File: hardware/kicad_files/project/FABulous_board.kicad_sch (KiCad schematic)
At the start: 7 parts, among them SW1 Tactile Switch

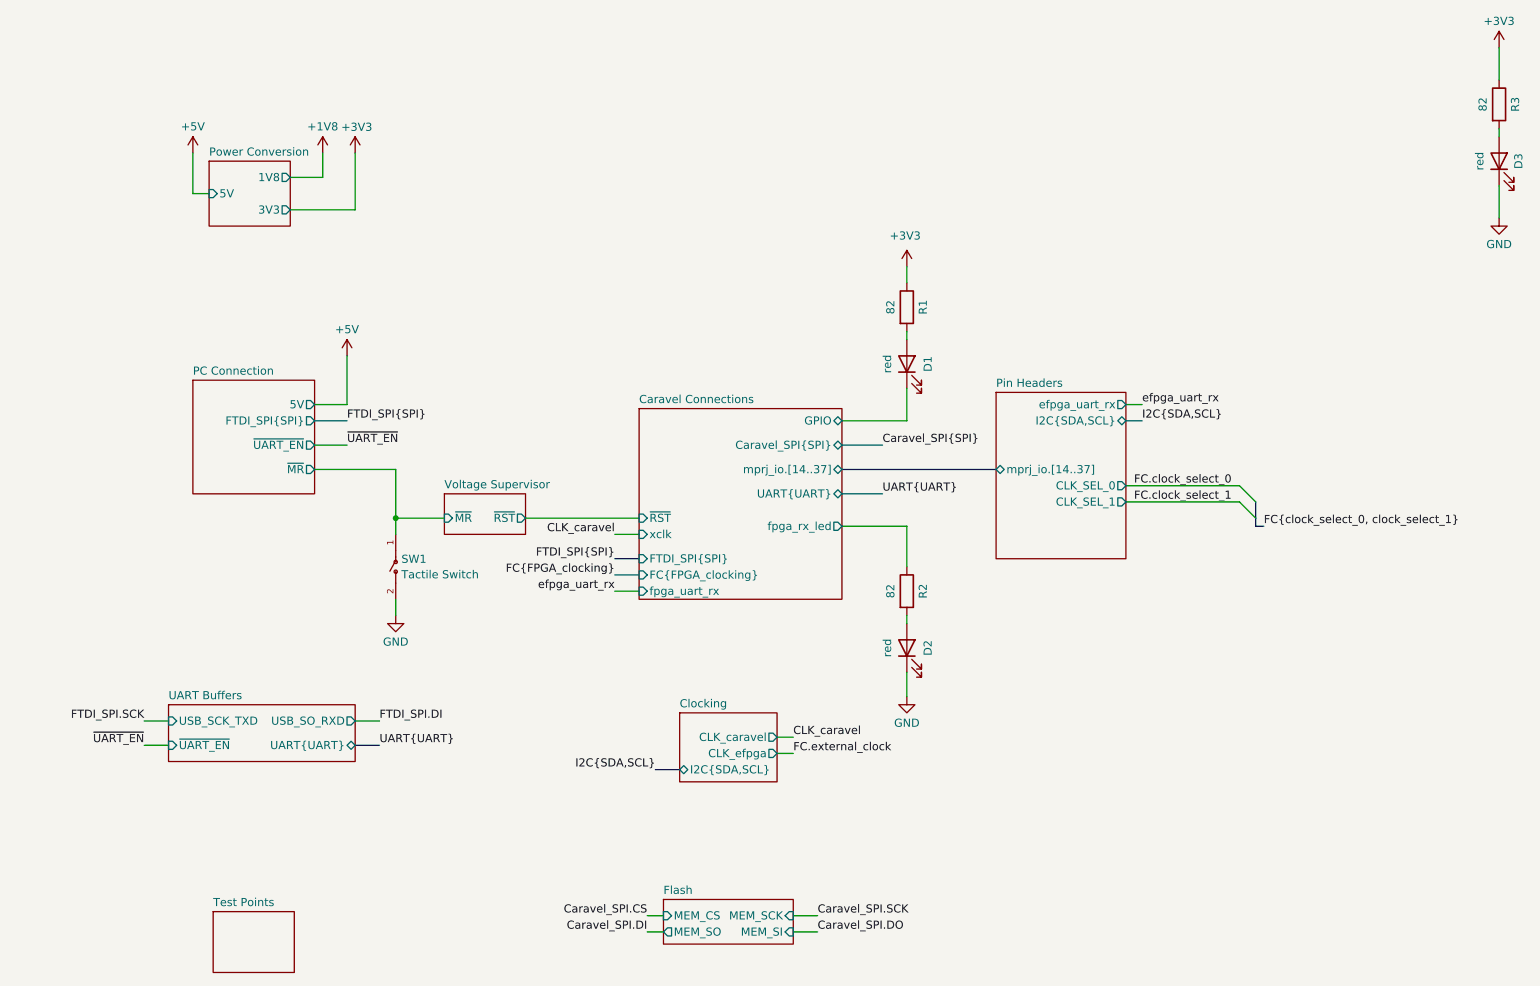
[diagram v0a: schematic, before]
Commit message: feat: optimize layout, reassign annotations, add 2x4 header for UART selection
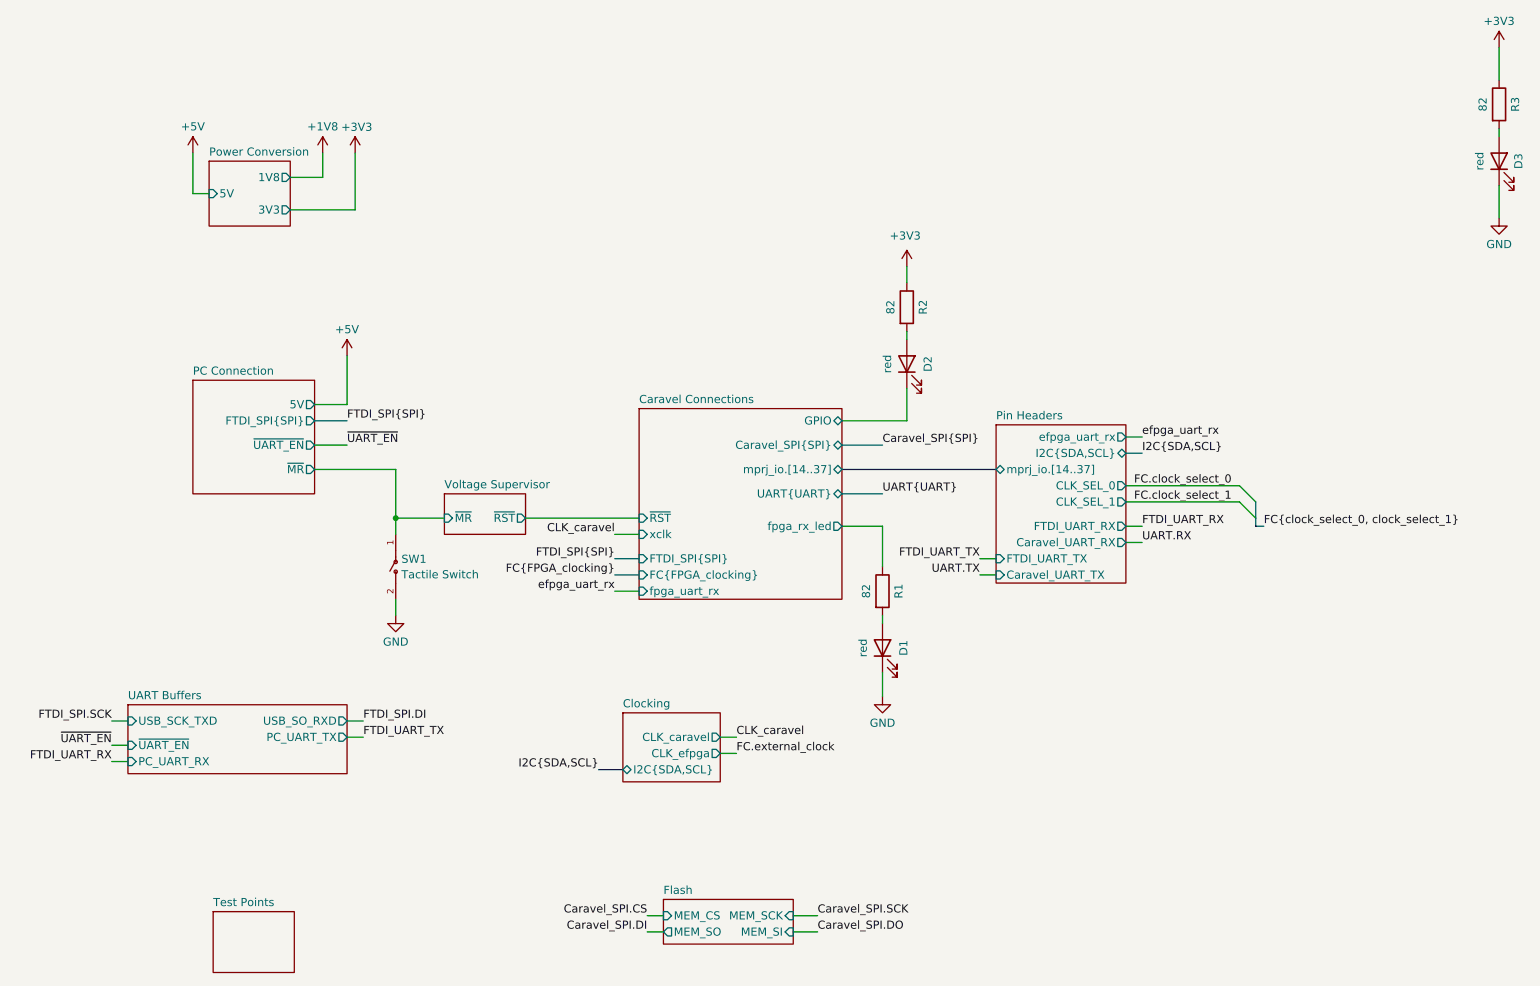
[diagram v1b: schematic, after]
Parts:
- R1: renamed from R2; value 82 -> 82
- R2: renamed from R1; value 82 -> 82
- renumbered D2 to D1, D1 to D2
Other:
- sheet Pin Headers ports: added Caravel_UART_RX, Caravel_UART_TX, FTDI_UART_RX, FTDI_UART_TX; removed none
- sheet UART Buffers ports: added PC_UART_RX, PC_UART_TX; removed UART{UART}
- moved on the sheet: D1, R1

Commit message: feat: implemented all suggestions, logos still missing or incorrect
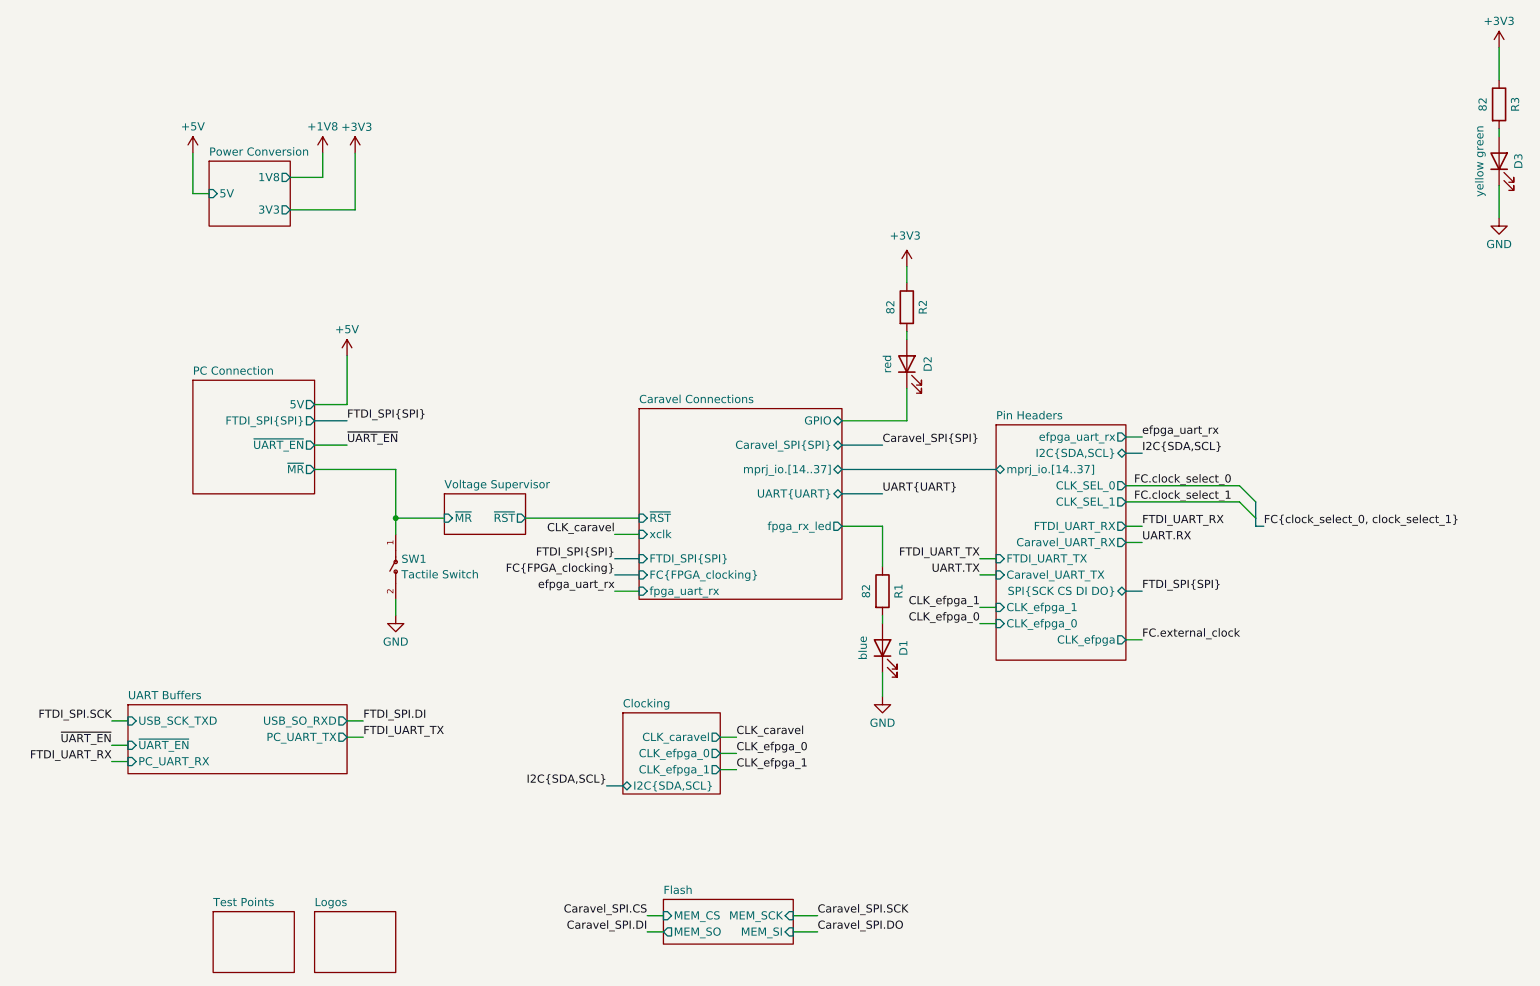
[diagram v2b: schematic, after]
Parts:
- D1: value red -> blue; LCSC Number (none) -> C434440
- D2: LCSC Number (none) -> XL-3216UGC-FB
- D3: value red -> yellow green; LCSC Number (none) -> C7496846
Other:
- added sheet Logos (logos.kicad_sch)
- sheet Clocking ports: added CLK_efpga_0, CLK_efpga_1; removed CLK_efpga
- sheet Pin Headers ports: added CLK_efpga, CLK_efpga_0, CLK_efpga_1, SPI{SCK CS DI DO}; removed none

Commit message: feat: Implement all findings of the second review
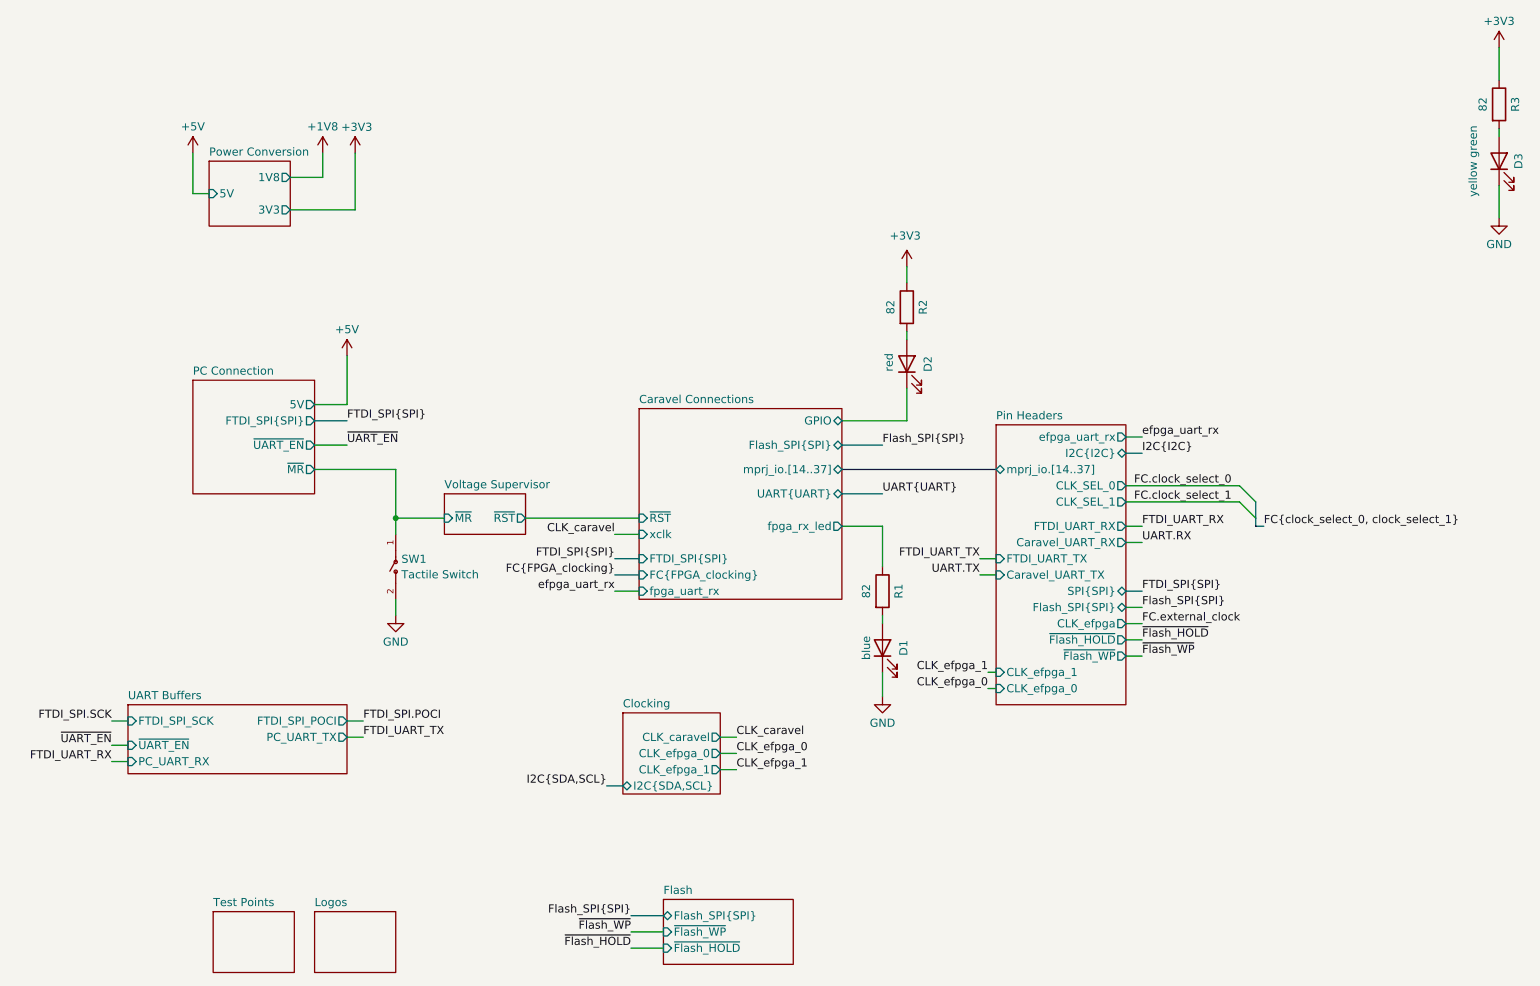
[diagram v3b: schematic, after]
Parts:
- D1: value blue -> C434440
- D2: value red -> C3646938
- D3: value yellow green -> C965826; LCSC (none) -> C965826; LCSC Number C7496846 -> (none)
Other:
- sheet Caravel Connections ports: added Flash_SPI{SPI}; removed Caravel_SPI{SPI}
- sheet Flash ports: added Flash_SPI{SPI}, ~{Flash_HOLD}, ~{Flash_WP}; removed MEM_CS, MEM_SCK, MEM_SI, MEM_SO
- sheet Pin Headers ports: added Flash_SPI{SPI}, I2C{I2C}, SPI{SPI}, ~{Flash_HOLD}, ~{Flash_WP}; removed I2C{SDA,SCL}, SPI{SCK CS DI DO}
- sheet UART Buffers ports: added FTDI_SPI_POCI, FTDI_SPI_SCK; removed USB_SCK_TXD, USB_SO_RXD

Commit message: feat: apply changes not saved before previous commit
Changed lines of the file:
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@@
+		)
+	)
+	(bus
+		(pts
+			(xy 203.2 118.11) (xy 205.74 118.11)
+		)
+		(stroke
+			(width 0)
+			(type default)
 		)
 	)
@@
 		)
 		(stroke
-			(width 0)
-			(type default)
-		)
-	)
-	(wire
-		(pts
-			(xy 205.74 118.11) (xy 203.2 118.11)
-		)
-		(stroke

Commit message: fix: use correct footprint for LED D2
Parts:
- D2: footprint LED_SMD:LED_1206_3216Metric -> easy_eda:LED1206-RD_RED_LTST-C230CKT
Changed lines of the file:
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@@
 			)
 		)
-		(property "Footprint" "LED_SMD:LED_1206_3216Metric"
+		(property "Footprint" "easy_eda:LED1206-RD_RED_LTST-C230CKT"
 			(at 168.91 80.01 0)
 			(effects

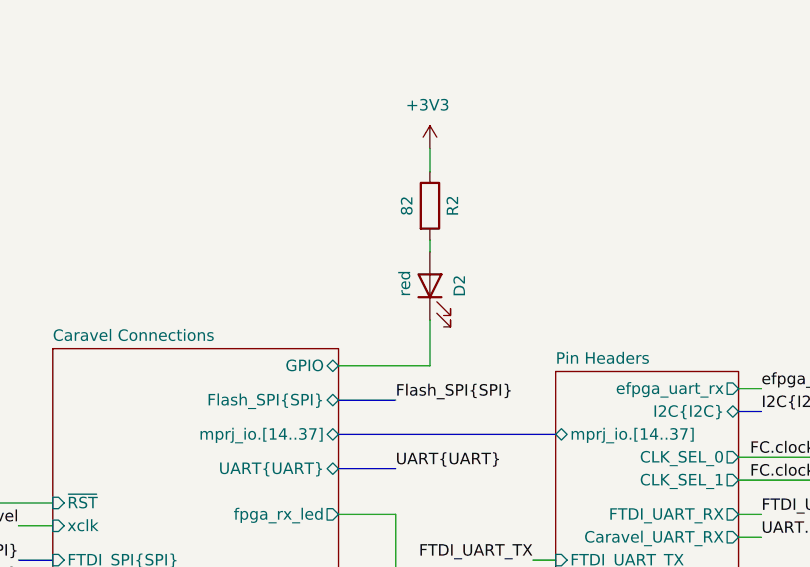
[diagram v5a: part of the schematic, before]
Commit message: fix D2 LED orientation and change Pads of USB-C connector to avoid warnings, also exlude all logos from BOM
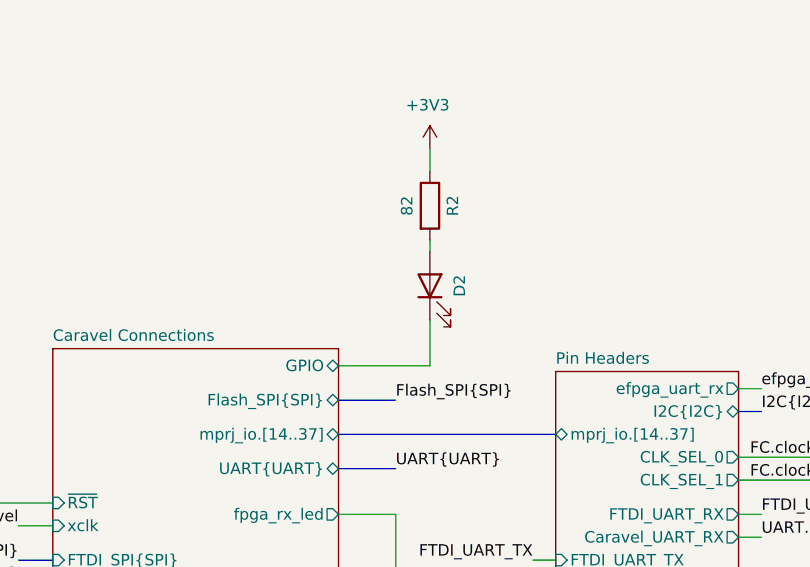
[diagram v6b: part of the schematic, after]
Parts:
- D2: value C3646938 -> C965822; footprint easy_eda:LED1206-RD_RED_LTST-C230CKT -> easy_eda:LED1206-R-RD_RED; JLCPCB Rotation Offset (none) -> 180; LCSC Number XL-3216UGC-FB -> C3646937
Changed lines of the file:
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@@
 			)
 		)
-		(property "Value" "C3646938"
+		(property "Value" "C965822"
 			(at 165.862 80.01 0)
 			(effects
@@
 			)
 		)
-		(property "Footprint" "easy_eda:LED1206-RD_RED_LTST-C230CKT"
+		(property "Footprint" "easy_eda:LED1206-R-RD_RED"
 			(at 168.91 80.01 0)
 			(effects
@@
 			)
 		)
-		(property "Description" "red"
-			(at 166.116 79.756 0)
+		(property "Description" "Light emitting diode"
+			(at 168.91 80.01 0)
 			(effects
 				(font
 					(size 1.27 1.27)
 				)
+				(hide yes)
 			)
 		)
-		(property "LCSC Number" "XL-3216UGC-FB"
+		(property "LCSC Number" " C3646937"
 			(at 168.91 80.01 0)
 			(effects
+				(font
+					(size 1.27 1.27)
+				)
+				(hide yes)
+			)
+		)
+		(property "JLCPCB Rotation Offset" "180"
+			(at 168.91 80.01 0)
+			(effects

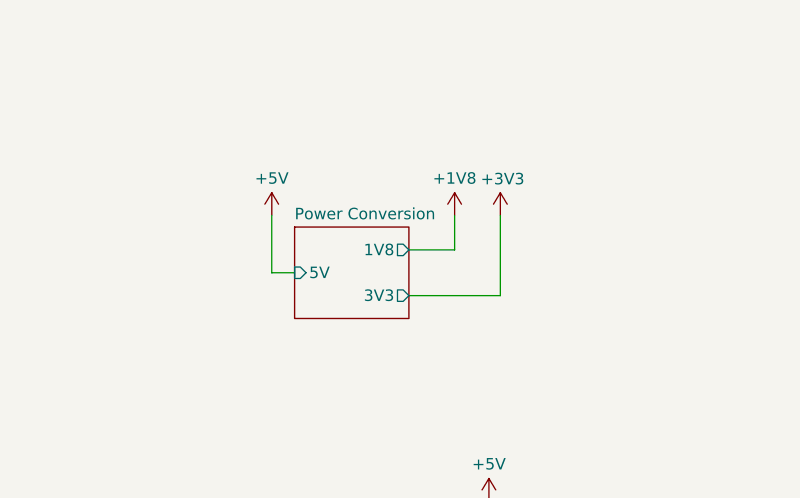
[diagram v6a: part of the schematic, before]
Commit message: fix: rename and reconnect S_DATA and S_CLK
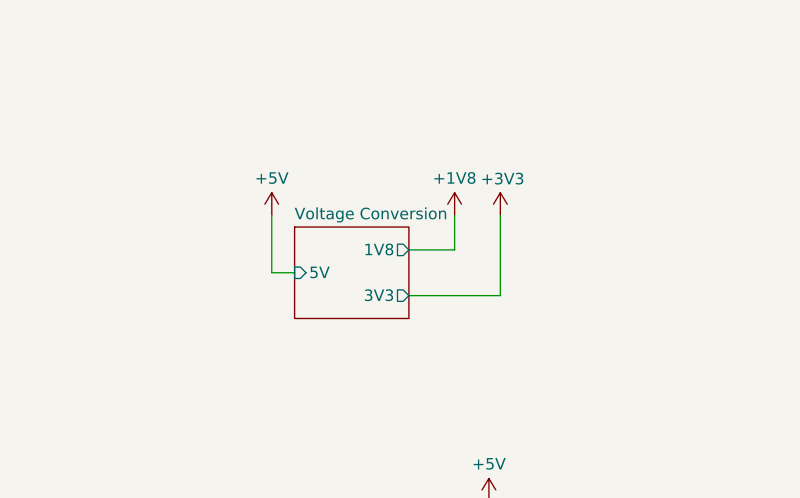
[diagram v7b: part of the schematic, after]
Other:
- sheet Power Conversion renamed Voltage Conversion
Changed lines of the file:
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@@
 			(color 0 0 0 0.0000)
 		)
-		(property "Sheetname" "Power Conversion"
+		(property "Sheetname" "Voltage Conversion"
 			(at 59.69 47.5484 0)
 			(effects
